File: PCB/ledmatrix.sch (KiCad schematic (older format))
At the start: 160 parts

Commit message: Updating schematic to use STM32F303CC microcontroller instead of ATMEGA32U4; next steps: swapping out USB3 interconnect for HDMI.
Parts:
- CLED11, CLED12, CLED13, CLED14, CLED15, CLED16, CLED17, CLED18, CLED19, CLED2, CLED20, CLED3, CLED4, CLED5, CLED6, CLED7, CLED8, CLED9: symbol C -> TS65-rescue:C
- LED1:1, LED1:10, LED1:11, LED1:12, LED1:13, LED1:14, LED1:15, LED1:15_2, LED1:16, LED1:2, LED1:3, LED1:4, LED1:5, LED1:6, LED1:7, LED1:8, LED1:9, LED2:1, LED2:10, LED2:11, LED2:12, LED2:13, LED2:14, LED2:15, LED2:16, LED2:2, LED2:3, LED2:4, LED2:5, LED2:6, LED2:8, LED2:9, LED3:10, LED3:11, LED3:12, LED3:13, LED3:14, LED3:15, LED3:15_2, LED3:15_3, LED3:16, LED3:2, LED3:3, LED3:4, LED3:5, LED3:6, LED3:8, LED3:9, LED4:1, LED4:10, LED4:11, LED4:12, LED4:13, LED4:13_2, LED4:15, LED4:16, LED4:1_2, LED4:2, LED4:3, LED4:4, LED4:5, LED4:6, LED4:7, LED4:8, LED4:9, LED5:1, LED5:10, LED5:10_2, LED5:10_3, LED5:10_4, LED5:10_5, LED5:10_6, LED5:10_7, LED5:11, LED5:11_2, LED5:11_3, LED5:11_4, LED5:11_5, LED5:12, LED5:12_2, LED5:12_3, LED5:13, LED5:13_2, LED5:15, LED5:15_2, LED5:16, LED5:1_2, LED5:2, LED5:2_2, LED5:2_3, LED5:3, LED5:3_2, LED5:3_3, LED5:3_4, LED5:4, LED5:4_2, LED5:4_3, LED5:4_4, LED5:4_5, LED5:4_6, LED5:4_7, LED5:5, LED5:5_2, LED5:5_3, LED5:5_4, LED5:8, LED5:8_2, LED5:8_3, LEDCL1, LEDCL2, LEDI1, LEDI1_2, LEDI2, LEDI2_2, LEDI3, LEDI3_2, LEDI4: symbol LED -> TS65-rescue:LED
- LEDG11, LEDG12, LEDG13, LEDG14, LEDG15, LEDG16, LEDG17, LEDG18, LEDG19, LEDG2, LEDG20, LEDG3, LEDG4, LEDG5, LEDG6, LEDG7, LEDG8, LEDG9: symbol WS2812B -> TS65-rescue:WS2812B
- R23, R24, RCL1, RI1, RI2, RI3, RI4: symbol R -> TS65-rescue:R

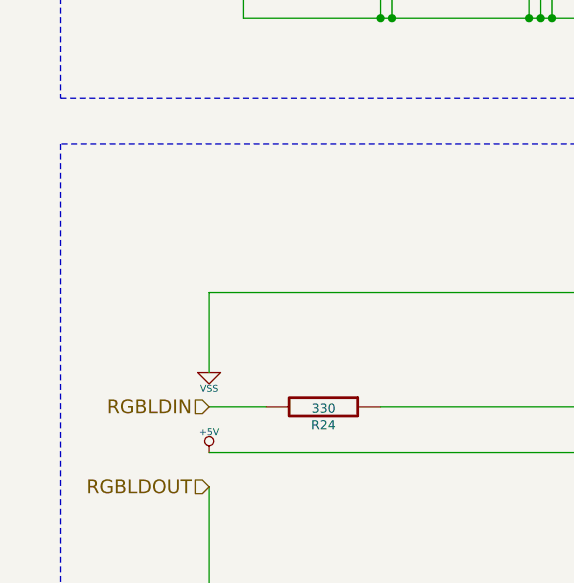
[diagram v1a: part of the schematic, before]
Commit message: Updating design to use STM32F303 instead of AVR32u4.
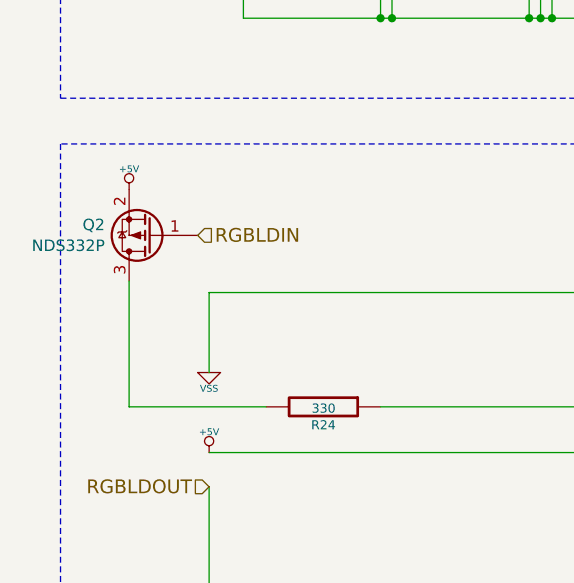
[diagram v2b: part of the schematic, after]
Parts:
- added Q2: NDS332P, prettylib:SOT-23, symbol Device:Q_PMOS_GSD
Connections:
- net +5V: now also Q2.2 (S)
- net RGBLDIN: now also Q2.1 (G); no longer R24.2
- new net: Q2.3 (D), R24.2
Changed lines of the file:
@@
 	1    0    0    -1
 $EndComp
-Text HLabel 1500 6200 0    60   Input ~ 0
+Text HLabel 1450 5450 2    60   Input ~ 0
 RGBLDIN
 Text HLabel 8650 6150 0    60   Input ~ 0
@@
 Wire Wire Line
 	3200 6800 3300 6800
-Wire Wire Line
-	1500 6200 1750 6200
 Connection ~ 6000 5700
 Wire Wire Line
@@
 Wire Wire Line
 	6600 5700 7100 5700
+$Comp
+L Device:Q_PMOS_GSD Q2
+U 1 1 5BD5D292
+P 1250 5450
+F 0 "Q2" H 1456 5404 50  0000 L CNN
+F 1 "NDS332P" H 1456 5495 50  0000 L CNN
+F 2 "prettylib:SOT-23" H 1450 5550 50  0001 C CNN
+F 3 "~" H 1250 5450 50  0001 C CNN
+	1    1250 5450
+	-1   0    0    1
+$EndComp
+$Comp
+L TS65-rescue:+5V #PWR0112
+U 1 1 5BD5D81C
+P 1150 5250
+F 0 "#PWR0112" H 1150 5340 20  0001 C CNN
+F 1 "+5V" H 1150 5340 30  0000 C CNN
+F 2 "" H 1150 5250 60  0000 C CNN
+F 3 "" H 1150 5250 60  0000 C CNN
+	1    1150 5250
+	1    0    0    -1
+$EndComp
+Wire Wire Line
+	1150 6200 1150 5650
+Wire Wire Line
+	1150 6200 1750 6200
 $EndSCHEMATC
